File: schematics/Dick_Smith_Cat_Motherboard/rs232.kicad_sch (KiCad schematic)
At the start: 10 parts, among them J1 RS232

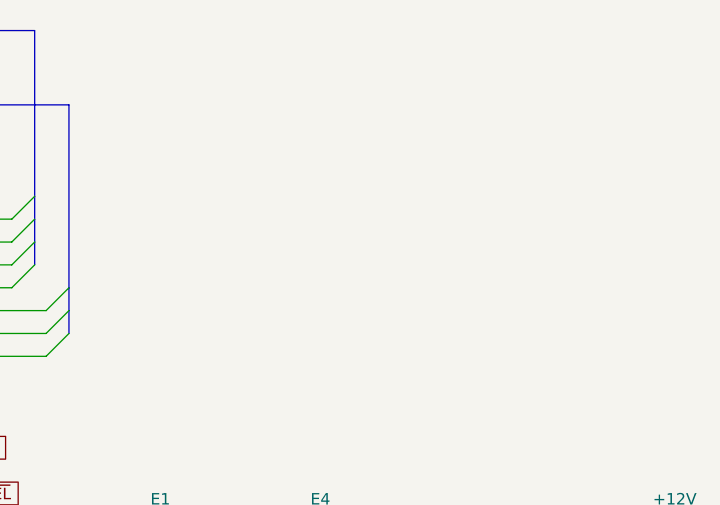
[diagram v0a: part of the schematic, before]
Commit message: Add more connector pinouts to the schematics
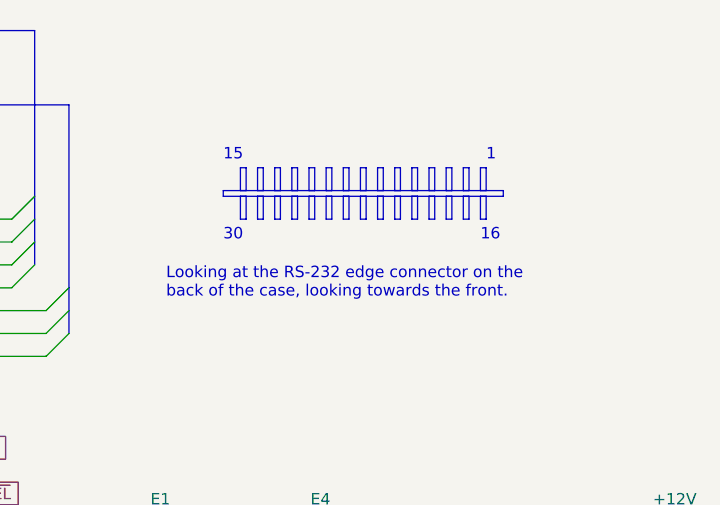
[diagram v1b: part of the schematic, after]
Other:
- note added: "1"
- note added: "15"
- note added: "16"
- note added: "30"
- note added: "Looking at the RS-232 edge connector on the back of the case, looking towards the front."
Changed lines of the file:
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@@
     (stroke (width 0) (type default))
+  )
+  (rectangle (start 224.79 76.835) (end 225.425 79.375)
+    (stroke (width 0) (type default))
+    (fill (type none))
+  )
+  (rectangle (start 219.075 76.835) (end 219.71 79.375)
+    (stroke (width 0) (type default))
+    (fill (type none))
+  )
+  (rectangle (start 213.36 73.66) (end 213.995 76.2)
+    (stroke (width 0) (type default))
+    (fill (type none))
+  )
+  (rectangle (start 203.835 73.66) (end 204.47 76.2)
+    (stroke (width 0) (type default))
+    (fill (type none))
+  )
+  (rectangle (start 222.885 76.835) (end 223.52 79.375)
+    (stroke (width 0) (type default))
+    (fill (type none))
+  )
+  (rectangle (start 205.74 73.66) (end 206.375 76.2)
+    (stroke (width 0) (type default))
+    (fill (type none))
+  )
+  (rectangle (start 201.93 73.66) (end 202.565 76.2)
+    (stroke (width 0) (type default))
+    (fill (type none))
+  )
+  (rectangle (start 217.17 73.66) (end 217.805 76.2)
+    (stroke (width 0) (type default))
+    (fill (type none))
+  )
+  (rectangle (start 207.645 73.66) (end 208.28 76.2)
+    (stroke (width 0) (type default))
+    (fill (type none))
+  )
+  (rectangle (start 203.835 76.835) (end 204.47 79.375)
+    (stroke (width 0) (type default))
+    (fill (type none))
+  )
+  (rectangle (start 209.55 76.835) (end 210.185 79.375)
+    (stroke (width 0) (type default))
+    (fill (type none))
+  )
+  (rectangle (start 200.025 73.66) (end 200.66 76.2)
+    (stroke (width 0) (type default))
+    (fill (type none))
+  )
+  (rectangle (start 215.265 76.835) (end 215.9 79.375)
+    (stroke (width 0) (type default))
+    (fill (type none))
+  )
+  (rectangle (start 198.12 76.835) (end 198.755 79.375)
+    (stroke (width 0) (type default))
+    (fill (type none))
+  )
+  (rectangle (start 220.98 73.66) (end 221.615 76.2)
+    (stroke (width 0) (type default))
+    (fill (type none))
+  )
+  (rectangle (start 222.885 73.66) (end 223.52 76.2)
+    (stroke (width 0) (type default))
+    (fill (type none))
+  )
+  (rectangle (start 220.98 76.835) (end 221.615 79.375)
+    (stroke (width 0) (type default))
+    (fill (type none))
+  )
+  (rectangle (start 211.455 73.66) (end 212.09 76.2)
+    (stroke (width 0) (type default))
+    (fill (type none))
+  )
+  (rectangle (start 200.025 76.835) (end 200.66 79.375)
+    (stroke (width 0) (type default))
+    (fill (type none))
+  )
+  (rectangle (start 211.455 76.835) (end 212.09 79.375)
+    (stroke (width 0) (type default))
+    (fill (type none))
+  )
+  (rectangle (start 213.36 76.835) (end 213.995 79.375)
+    (stroke (width 0) (type default))
+    (fill (type none))
+  )
+  (rectangle (start 217.17 76.835) (end 217.805 79.375)
+    (stroke (width 0) (type default))
+    (fill (type none))
+  )
+  (rectangle (start 205.74 76.835) (end 206.375 79.375)
+    (stroke (width 0) (type default))
+    (fill (type none))
+  )
+  (rectangle (start 196.215 76.2) (end 227.33 76.835)
+    (stroke (width 0) (type default))
+    (fill (type none))
+  )
+  (rectangle (start 207.645 76.835) (end 208.28 79.375)
+    (stroke (width 0) (type default))
+    (fill (type none))
+  )
+  (rectangle (start 201.93 76.835) (end 202.565 79.375)
+    (stroke (width 0) (type default))
+    (fill (type none))
+  )
+  (rectangle (start 215.265 73.66) (end 215.9 76.2)
+    (stroke (width 0) (type default))
+    (fill (type none))
+  )
+  (rectangle (start 224.79 73.66) (end 225.425 76.2)
+    (stroke (width 0) (type default))
+    (fill (type none))
+  )
+  (rectangle (start 198.12 73.66) (end 198.755 76.2)
+    (stroke (width 0) (type default))
+    (fill (type none))
+  )
+  (rectangle (start 209.55 73.66) (end 210.185 76.2)
+    (stroke (width 0) (type default))
+    (fill (type none))
+  )
+  (rectangle (start 219.075 73.66) (end 219.71 76.2)
+    (stroke (width 0) (type default))
+    (fill (type none))
+  )
+  (text "1" (at 225.425 73.025 0)
+    (effects (font (size 1.27 1.27)) (justify left bottom))
+  )
+  (text "Looking at the RS-232 edge connector on the\nback of the case, looking towards the front."
+    (at 189.865 88.265 0)
+    (effects (font (size 1.27 1.27)) (justify left bottom))
+  )
+  (text "15" (at 196.215 73.025 0)
+    (effects (font (size 1.27 1.27)) (justify left bottom))
+  )
+  (text "30" (at 196.215 81.915 0)
+    (effects (font (size 1.27 1.27)) (justify left bottom))
+  )
+  (text "16" (at 224.79 81.915 0)
+    (effects (font (size 1.27 1.27)) (justify left bottom))
   )
   (label "BD2" (at 164.465 86.995 0) (fields_autoplaced)
